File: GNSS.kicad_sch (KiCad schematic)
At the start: 24 parts, among them J61 USB_C_USB2.0_16P, J62 Micro_SD_Card, SW61 KMR2, U61 NEO-M9N

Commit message: Post-manufacturing v1 check.
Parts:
- C64: LCSC Part C307331 -> (none)
- C66: LCSC Part C1525 -> (none)
- R63: LCSC Part C17415 -> (none)
- SW61: LCSC Part C720477 -> (none)
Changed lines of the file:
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@@
 			)
 		)
-		(property "LCSC Part" "C17415"
+		(property "LCSC Part" ""
 			(at 152.4 57.15 0)
 			(effects
@@
 			)
 		)
-		(property "LCSC Part" "C720477"
+		(property "LCSC Part" ""
 			(at 76.2 99.06 0)
 			(effects
@@
 			)
 		)
-		(property "LCSC Part" "C307331"
+		(property "LCSC Part" ""
 			(at 165.1 69.85 0)
 			(effects
@@
 			)
 		)
-		(property "LCSC Part" "C1525"
+		(property "LCSC Part" ""
 			(at 66.04 171.45 0)
 			(effects

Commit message: Add 10k pull-ups to SDcard
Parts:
- added R64: 10k, Resistor_SMD:R_0402_1005Metric, symbol Device:R
- added RN61: 10k, Resistor_SMD:R_Array_Concave_4x0603, symbol Device:R_Pack04
- TP61: renamed from TP65; value TestPoint -> TP_DAT1
- TP62: renamed from TP66; value TestPoint -> TP_DAT2
- renumbered C66 to C61, C61 to C62, C65 to C63, C62 to C64, C63 to C65, C64 to C66, R66 to R61, R61 to R62, R62 to R63, R64 to R65, R65 to R66, R63 to R67, TP61 to TP63, TP62 to TP64, TP63 to TP65, TP64 to TP66
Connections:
- net +3V3: now also R64.2, RN61.6 (R3.2), RN61.7 (R2.2), RN61.8 (R1.2)
- net SPI_CS0: now also RN61.3 (R3.1)
- net SPI_CS1: now also R64.1
- net SPI_MISO: now also RN61.1 (R1.1)
- net SPI_MOSI: now also RN61.2 (R2.1)
- no-connect marks 3 -> 5
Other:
- note added: "DO NOT PULL UP SCK"
- note removed: "Decoupling for SD Card?"
- title: GNSS NEO-M9N -> GNSS NEO-M9N & MicroSD Card
- moved on the sheet: C61, C63, J62, TP61, TP62

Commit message: v2 layouts done
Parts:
- renumbered C61 to C63, C62 to C64, C63 to C65, C64 to C66, C65 to C67, C66 to C68, J61 to J41, J62 to J42, JP61 to JP31, L61 to L34, R61 to R66, R62 to R67, R63 to R68, R64 to R69, R65 to R70, R66 to R71, R67 to R72, RN61 to RN31, SW61 to SW34, TP61 to TP31, TP62 to TP32, TP63 to TP33, TP64 to TP34, TP65 to TP35, TP66 to TP36, U61 to U40

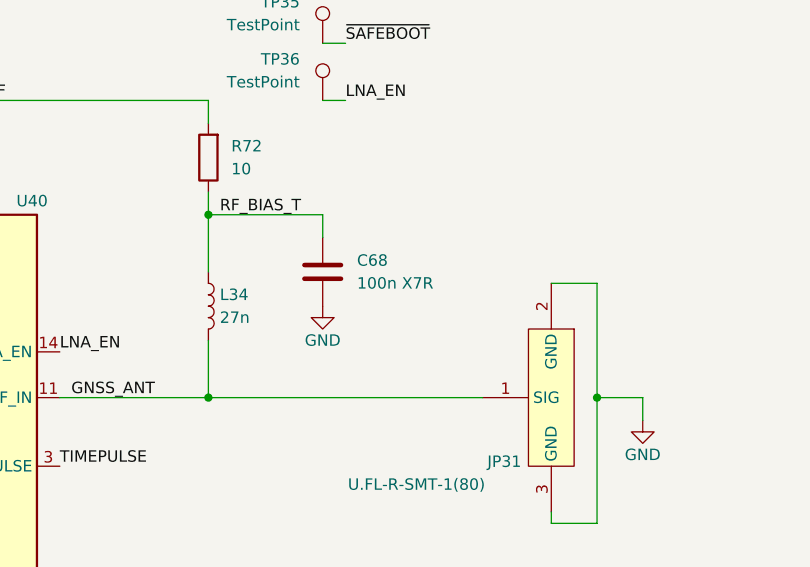
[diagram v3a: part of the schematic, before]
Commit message: Final production changes
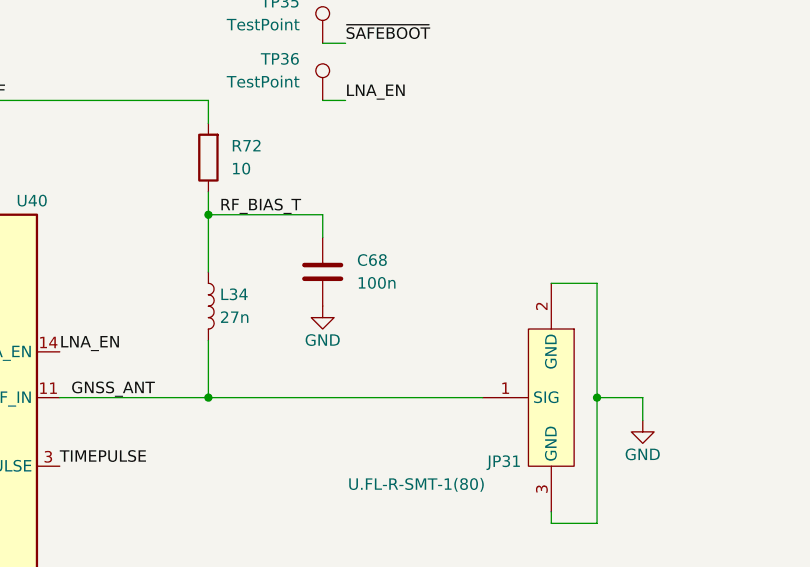
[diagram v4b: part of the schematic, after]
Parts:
- C68: value 100n X7R -> 100n
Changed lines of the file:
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@@
 			)
 		)
-		(property "Value" "100n X7R"
+		(property "Value" "100n"
 			(at 168.91 71.1199 0)
 			(effects
